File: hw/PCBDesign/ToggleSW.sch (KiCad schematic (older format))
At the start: 8 parts

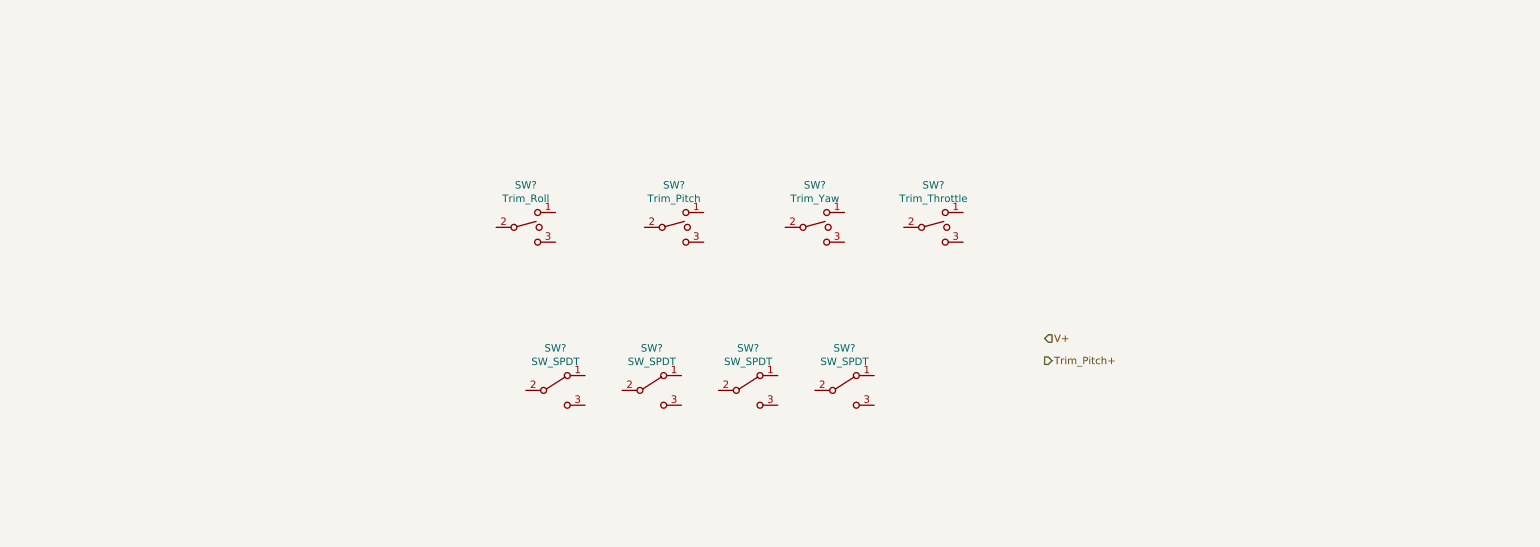
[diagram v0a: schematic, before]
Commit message: Add HMI input circuitry
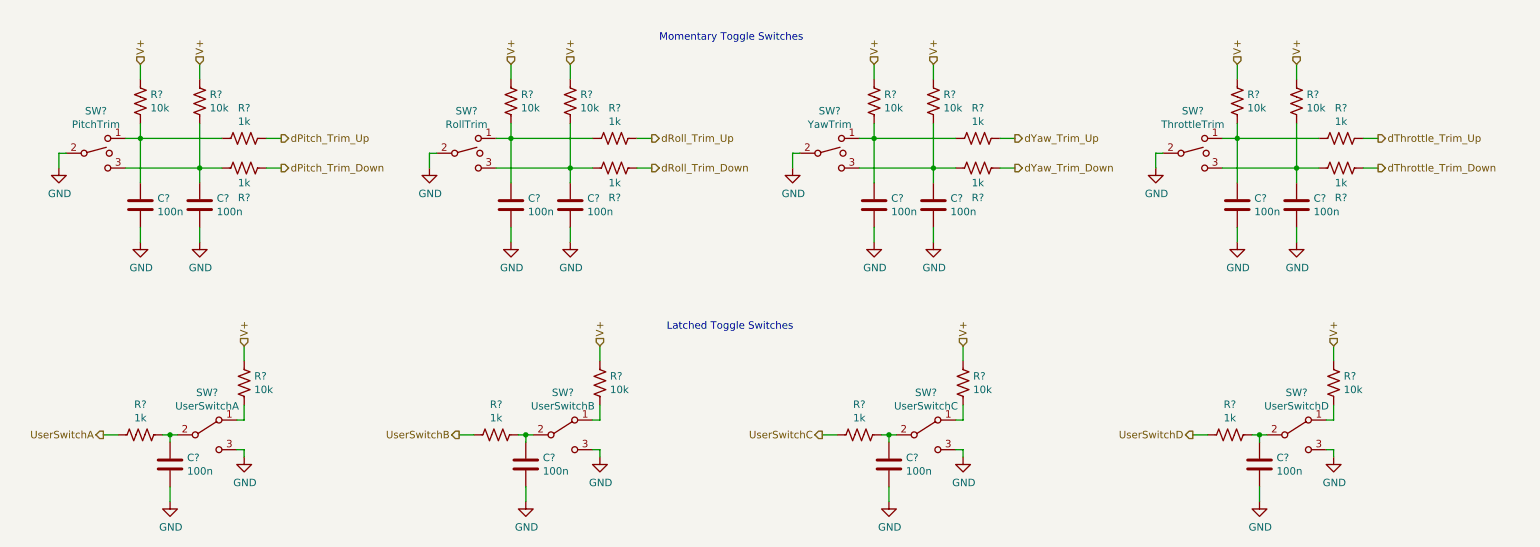
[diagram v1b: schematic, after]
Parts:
- removed SW?: Trim_Pitch, symbol Switch:SW_SPDT_MSM
- removed SW?: Trim_Yaw, symbol Switch:SW_SPDT_MSM
- removed SW?: Trim_Throttle, symbol Switch:SW_SPDT_MSM
- removed SW? (x3): SW_SPDT, symbol Switch:SW_SPDT
- added C? (x12): 100n, symbol Device:C
- added R? (x12): 10k, symbol Device:R_US
- added R? (x12): 1k, symbol Device:R_US
- added SW?: RollTrim, symbol Switch:SW_SPDT_MSM
- added SW?: YawTrim, symbol Switch:SW_SPDT_MSM
- added SW?: ThrottleTrim, symbol Switch:SW_SPDT_MSM
- added SW?: UserSwitchB, symbol Switch:SW_SPDT
- added SW?: UserSwitchC, symbol Switch:SW_SPDT
- added SW?: UserSwitchD, symbol Switch:SW_SPDT
- SW?: value Trim_Roll -> PitchTrim
- SW?: value SW_SPDT -> UserSwitchA
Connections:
- net V+: now also R?.1, R?.1, R?.1, R?.1, R?.1, R?.1, R?.1, R?.1, R?.1, R?.1, R?.1, R?.1
- net at SW?.1: now also C?.1, R?.2, R?.2
- net GND: now reaches SW?.2
- net GND: now also SW?.3 (C), C?.2, C?.2, C?.2, C?.2, C?.2, C?.2, C?.2, C?.2, C?.2, C?.2, C?.2, C?.2, SW?.2, SW?.2, SW?.2, SW?.3 (C), SW?.3 (C), SW?.3 (C)
- net at SW?.3: now also C?.1, R?.1, R?.2
- net at SW?.1 (A): now also R?.2
- net at SW?.2 (B): now also C?.1, R?.1
- new net: C?.1, R?.2, R?.2, SW?.1 (x3)
- new net: C?.1, R?.1, R?.2, SW?.3 (x3)
- new net: R?.2, SW?.1 (A) (x3)
- new net: C?.1, R?.1, SW?.2 (B) (x3)
- new net UserSwitchA: R?.2
- new net UserSwitchB: R?.2
- new net UserSwitchC: R?.2
- new net UserSwitchD: R?.2
- new net dPitch_Trim_Down: R?.2
- new net dPitch_Trim_Up: R?.1
- new net dRoll_Trim_Down: R?.2
- new net dRoll_Trim_Up: R?.1
- new net dThrottle_Trim_Down: R?.2
- new net dThrottle_Trim_Up: R?.1
- new net dYaw_Trim_Down: R?.2
- new net dYaw_Trim_Up: R?.1
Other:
- note added: "Latched Toggle Switches"
- note added: "Momentary Toggle Switches"
- moved on the sheet: SW?

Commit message: Schematic polishing
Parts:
- added J10, J11, J12, J13, J14, J7, J8, J9: Conn_01x03, symbol Connector_Generic:Conn_01x03
- C10, C11, C12, C13, C14, C15, C16, C17, C18, C19, C20, C21: renamed from C?; footprint (none) -> Capacitor_SMD:C_0402_1005Metric; LCSC (none) -> C1525
- R15, R17, R20, R22, R23, R24, R28, R29, R30, R34, R35, R36: renamed from R?; footprint (none) -> Resistor_SMD:R_0402_1005Metric; LCSC (none) -> C25744
- R16, R18, R19, R21, R25, R26, R27, R31, R32, R33, R37, R38: renamed from R?; footprint (none) -> Resistor_SMD:R_0402_1005Metric; LCSC (none) -> C11702
- gave numbers to parts that had none: 8
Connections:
- net GND: now also J10.3 (Pin_3), J11.2 (Pin_2), J12.3 (Pin_3), J13.2 (Pin_2), J14.3 (Pin_3), J7.2 (Pin_2), J8.3 (Pin_3), J9.2 (Pin_2)
- net at C10.1, R15.2, R18.2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: now also J7.3 (Pin_3)
- net at C12.1, R17.2, R19.1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: now also J7.1 (Pin_1)
- net at R20.2, SW4.1 (A): now also J8.1 (Pin_1)
- net at C11.1, R16.1, SW4.2 (B): now also J8.2 (Pin_2)
- net at C13.1, R22.2, R25.2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: now also J9.3 (Pin_3)
- net at C15.1, R23.2, R26.1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: now also J9.1 (Pin_1)
- net at C16.1, R28.2, R31.2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: now also J11.3 (Pin_3)
- net at C18.1, R29.2, R32.1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: now also J11.1 (Pin_1)
- net at C19.1, R34.2, R37.2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: now also J13.3 (Pin_3)
- net at C21.1, R35.2, R38.1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: now also J13.1 (Pin_1)
- net at R24.2, SW6.1 (A): now also J10.1 (Pin_1)
- net at C14.1, R21.1, SW6.2 (B): now also J10.2 (Pin_2)
- net at R30.2, SW8.1 (A): now also J12.1 (Pin_1)
- net at C17.1, R27.1, SW8.2 (B): now also J12.2 (Pin_2)
- net at R36.2, SW10.1 (A): now also J14.1 (Pin_1)
- net at C20.1, R33.1, SW10.2 (B): now also J14.2 (Pin_2)

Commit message: Added PCB
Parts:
- J10, J11, J12, J13, J14, J7, J8, J9: footprint (none) -> Connector_JST:JST_PH_S3B-PH-SM4-TB_1x03-1MP_P2.00mm_Horizontal; DigiKey (none) -> 455-1750-2-ND
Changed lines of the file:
@@
 F 0 "J14" H 10030 3592 50  0000 L CNN
 F 1 "Conn_01x03" H 10030 3501 50  0000 L CNN
-F 2 "" H 9950 3550 50  0001 C CNN
+F 2 "Connector_JST:JST_PH_S3B-PH-SM4-TB_1x03-1MP_P2.00mm_Horizontal" H 9950 3550 50  0001 C CNN
 F 3 "~" H 9950 3550 50  0001 C CNN
+F 4 "455-1750-2-ND" H 9950 3550 50  0001 C CNN "DigiKey"
 	1    9950 3550
 	1    0    0    -1
@@
 F 0 "J12" H 7530 3592 50  0000 L CNN
 F 1 "Conn_01x03" H 7530 3501 50  0000 L CNN
-F 2 "" H 7450 3550 50  0001 C CNN
+F 2 "Connector_JST:JST_PH_S3B-PH-SM4-TB_1x03-1MP_P2.00mm_Horizontal" H 7450 3550 50  0001 C CNN
 F 3 "~" H 7450 3550 50  0001 C CNN
+F 4 "455-1750-2-ND" H 7450 3550 50  0001 C CNN "DigiKey"
 	1    7450 3550
 	1    0    0    -1
@@
 F 0 "J10" H 5080 3592 50  0000 L CNN
 F 1 "Conn_01x03" H 5080 3501 50  0000 L CNN
-F 2 "" H 5000 3550 50  0001 C CNN
+F 2 "Connector_JST:JST_PH_S3B-PH-SM4-TB_1x03-1MP_P2.00mm_Horizontal" H 5000 3550 50  0001 C CNN
 F 3 "~" H 5000 3550 50  0001 C CNN
+F 4 "455-1750-2-ND" H 5000 3550 50  0001 C CNN "DigiKey"
 	1    5000 3550
 	1    0    0    -1
@@
 F 0 "J8" H 2680 3592 50  0000 L CNN
 F 1 "Conn_01x03" H 2680 3501 50  0000 L CNN
-F 2 "" H 2600 3550 50  0001 C CNN
+F 2 "Connector_JST:JST_PH_S3B-PH-SM4-TB_1x03-1MP_P2.00mm_Horizontal" H 2600 3550 50  0001 C CNN
 F 3 "~" H 2600 3550 50  0001 C CNN
+F 4 "455-1750-2-ND" H 2600 3550 50  0001 C CNN "DigiKey"
 	1    2600 3550
 	1    0    0    -1
@@
 F 0 "J7" V 1864 930 50  0000 L CNN
 F 1 "Conn_01x03" V 1773 930 50  0000 L CNN
-F 2 "" H 1900 750 50  0001 C CNN
+F 2 "Connector_JST:JST_PH_S3B-PH-SM4-TB_1x03-1MP_P2.00mm_Horizontal" H 1900 750 50  0001 C CNN
 F 3 "~" H 1900 750 50  0001 C CNN
+F 4 "455-1750-2-ND" H 1900 750 50  0001 C CNN "DigiKey"
 	1    1900 750
 	0    1    -1   0
@@
 F 0 "J9" V 4364 930 50  0000 L CNN
 F 1 "Conn_01x03" V 4273 930 50  0000 L CNN
-F 2 "" H 4400 750 50  0001 C CNN
+F 2 "Connector_JST:JST_PH_S3B-PH-SM4-TB_1x03-1MP_P2.00mm_Horizontal" H 4400 750 50  0001 C CNN
 F 3 "~" H 4400 750 50  0001 C CNN
+F 4 "455-1750-2-ND" H 4400 750 50  0001 C CNN "DigiKey"
 	1    4400 750
 	0    1    -1   0
@@
 F 0 "J11" V 6814 930 50  0000 L CNN
 F 1 "Conn_01x03" V 6723 930 50  0000 L CNN
-F 2 "" H 6850 750 50  0001 C CNN
+F 2 "Connector_JST:JST_PH_S3B-PH-SM4-TB_1x03-1MP_P2.00mm_Horizontal" H 6850 750 50  0001 C CNN
 F 3 "~" H 6850 750 50  0001 C CNN
+F 4 "455-1750-2-ND" H 6850 750 50  0001 C CNN "DigiKey"
 	1    6850 750
 	0    1    -1   0
@@
 F 0 "J13" V 9264 930 50  0000 L CNN
 F 1 "Conn_01x03" V 9173 930 50  0000 L CNN
-F 2 "" H 9300 750 50  0001 C CNN
+F 2 "Connector_JST:JST_PH_S3B-PH-SM4-TB_1x03-1MP_P2.00mm_Horizontal" H 9300 750 50  0001 C CNN
 F 3 "~" H 9300 750 50  0001 C CNN
+F 4 "455-1750-2-ND" H 9300 750 50  0001 C CNN "DigiKey"
 	1    9300 750
 	0    1    -1   0

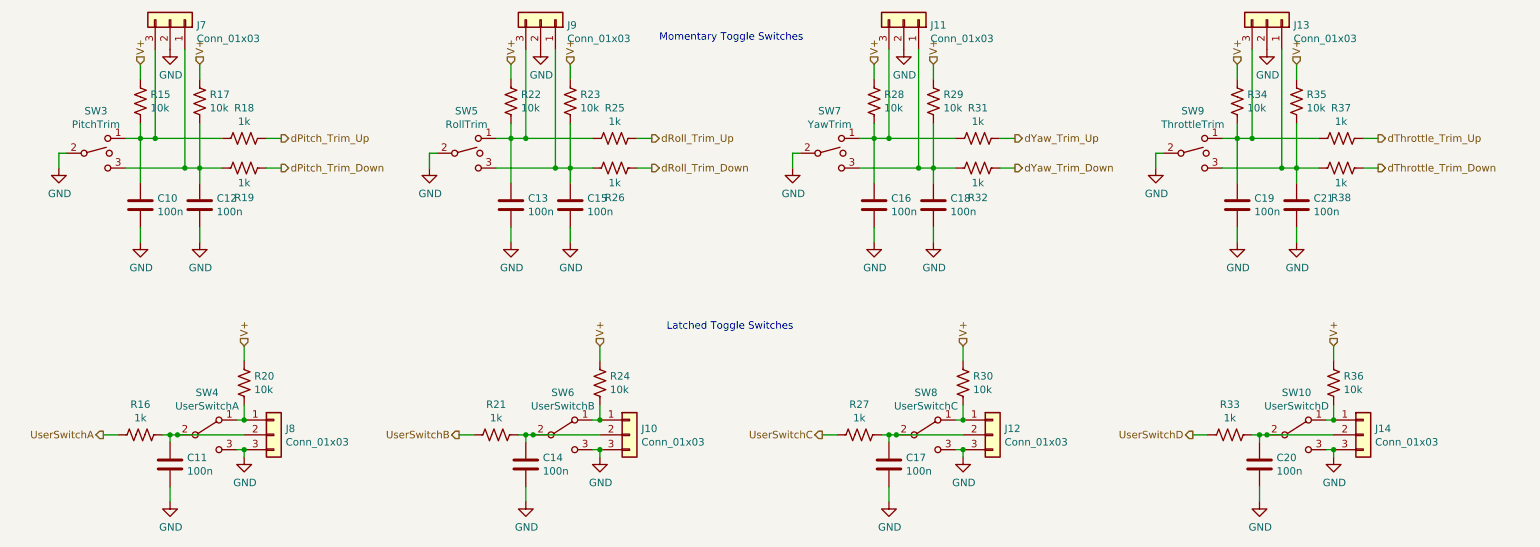
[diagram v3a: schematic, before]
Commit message: Laid out power section
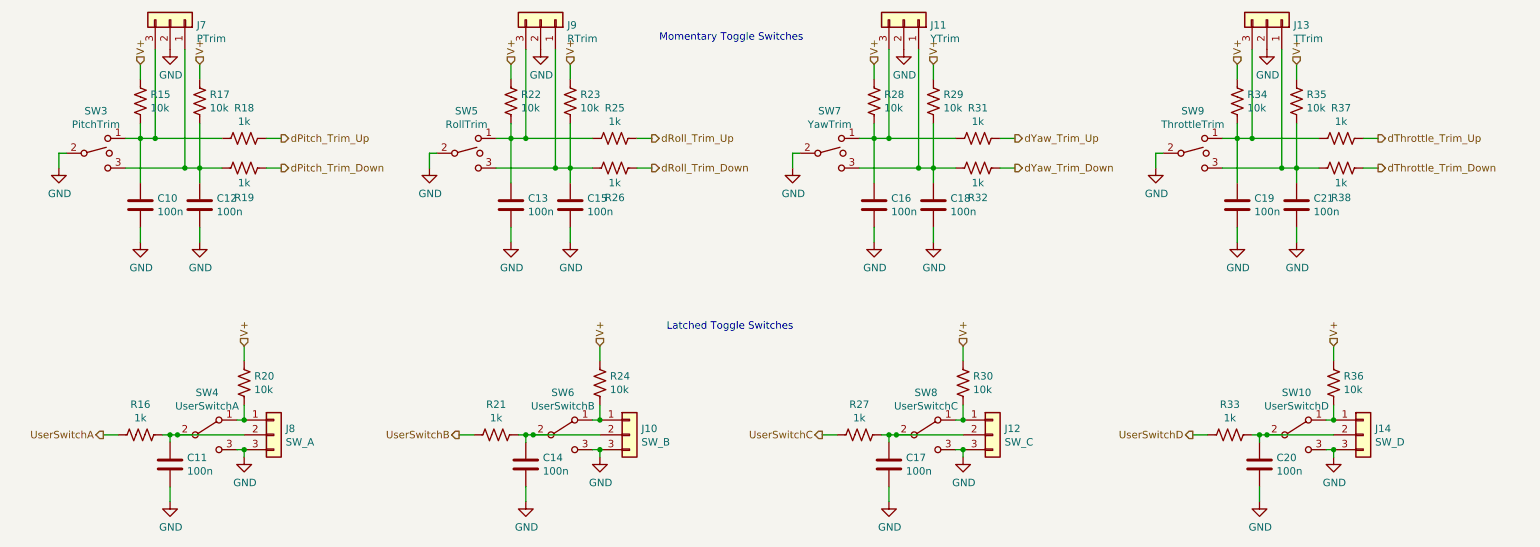
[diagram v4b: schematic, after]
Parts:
- J10: value Conn_01x03 -> SW_B
- J11: value Conn_01x03 -> YTrim
- J12: value Conn_01x03 -> SW_C
- J13: value Conn_01x03 -> TTrim
- J14: value Conn_01x03 -> SW_D
- J7: value Conn_01x03 -> PTrim
- J8: value Conn_01x03 -> SW_A
- J9: value Conn_01x03 -> RTrim
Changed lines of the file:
@@
 P 9950 3550
 F 0 "J14" H 10030 3592 50  0000 L CNN
-F 1 "Conn_01x03" H 10030 3501 50  0000 L CNN
+F 1 "SW_D" H 10030 3501 50  0000 L CNN
 F 2 "Connector_JST:JST_PH_S3B-PH-SM4-TB_1x03-1MP_P2.00mm_Horizontal" H 9950 3550 50  0001 C CNN
 F 3 "~" H 9950 3550 50  0001 C CNN
@@
 P 7450 3550
 F 0 "J12" H 7530 3592 50  0000 L CNN
-F 1 "Conn_01x03" H 7530 3501 50  0000 L CNN
+F 1 "SW_C" H 7530 3501 50  0000 L CNN
 F 2 "Connector_JST:JST_PH_S3B-PH-SM4-TB_1x03-1MP_P2.00mm_Horizontal" H 7450 3550 50  0001 C CNN
 F 3 "~" H 7450 3550 50  0001 C CNN
@@
 P 5000 3550
 F 0 "J10" H 5080 3592 50  0000 L CNN
-F 1 "Conn_01x03" H 5080 3501 50  0000 L CNN
+F 1 "SW_B" H 5080 3501 50  0000 L CNN
 F 2 "Connector_JST:JST_PH_S3B-PH-SM4-TB_1x03-1MP_P2.00mm_Horizontal" H 5000 3550 50  0001 C CNN
 F 3 "~" H 5000 3550 50  0001 C CNN
@@
 P 2600 3550
 F 0 "J8" H 2680 3592 50  0000 L CNN
-F 1 "Conn_01x03" H 2680 3501 50  0000 L CNN
+F 1 "SW_A" H 2680 3501 50  0000 L CNN
 F 2 "Connector_JST:JST_PH_S3B-PH-SM4-TB_1x03-1MP_P2.00mm_Horizontal" H 2600 3550 50  0001 C CNN
 F 3 "~" H 2600 3550 50  0001 C CNN
@@
 P 1900 750
 F 0 "J7" V 1864 930 50  0000 L CNN
-F 1 "Conn_01x03" V 1773 930 50  0000 L CNN
+F 1 "PTrim" V 1773 930 50  0000 L CNN
 F 2 "Connector_JST:JST_PH_S3B-PH-SM4-TB_1x03-1MP_P2.00mm_Horizontal" H 1900 750 50  0001 C CNN
 F 3 "~" H 1900 750 50  0001 C CNN
@@
 P 4400 750
 F 0 "J9" V 4364 930 50  0000 L CNN
-F 1 "Conn_01x03" V 4273 930 50  0000 L CNN
+F 1 "RTrim" V 4273 930 50  0000 L CNN
 F 2 "Connector_JST:JST_PH_S3B-PH-SM4-TB_1x03-1MP_P2.00mm_Horizontal" H 4400 750 50  0001 C CNN
 F 3 "~" H 4400 750 50  0001 C CNN
@@
 P 6850 750
 F 0 "J11" V 6814 930 50  0000 L CNN
-F 1 "Conn_01x03" V 6723 930 50  0000 L CNN
+F 1 "YTrim" V 6723 930 50  0000 L CNN
 F 2 "Connector_JST:JST_PH_S3B-PH-SM4-TB_1x03-1MP_P2.00mm_Horizontal" H 6850 750 50  0001 C CNN
 F 3 "~" H 6850 750 50  0001 C CNN
@@
 P 9300 750
 F 0 "J13" V 9264 930 50  0000 L CNN
-F 1 "Conn_01x03" V 9173 930 50  0000 L CNN
+F 1 "TTrim" V 9173 930 50  0000 L CNN
 F 2 "Connector_JST:JST_PH_S3B-PH-SM4-TB_1x03-1MP_P2.00mm_Horizontal" H 9300 750 50  0001 C CNN
 F 3 "~" H 9300 750 50  0001 C CNN

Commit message: HW updates. Testing out SPIFFS
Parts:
- J10, J11, J12, J13, J14, J7, J8, J9: footprint Connector_JST:JST_PH_S3B-PH-SM4-TB_1x03-1MP_P2.00mm_Horizontal -> Connector_JST:JST_PH_B3B-PH-SM4-TB_1x03-1MP_P2.00mm_Vertical; DigiKey 455-1750-2-ND -> 455-1735-2-ND
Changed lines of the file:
@@
 F 0 "J14" H 10030 3592 50  0000 L CNN
 F 1 "SW_D" H 10030 3501 50  0000 L CNN
-F 2 "Connector_JST:JST_PH_S3B-PH-SM4-TB_1x03-1MP_P2.00mm_Horizontal" H 9950 3550 50  0001 C CNN
+F 2 "Connector_JST:JST_PH_B3B-PH-SM4-TB_1x03-1MP_P2.00mm_Vertical" H 9950 3550 50  0001 C CNN
 F 3 "~" H 9950 3550 50  0001 C CNN
-F 4 "455-1750-2-ND" H 9950 3550 50  0001 C CNN "DigiKey"
+F 4 "455-1735-2-ND" H 9950 3550 50  0001 C CNN "DigiKey"
 	1    9950 3550
 	1    0    0    -1
@@
 F 0 "J12" H 7530 3592 50  0000 L CNN
 F 1 "SW_C" H 7530 3501 50  0000 L CNN
-F 2 "Connector_JST:JST_PH_S3B-PH-SM4-TB_1x03-1MP_P2.00mm_Horizontal" H 7450 3550 50  0001 C CNN
+F 2 "Connector_JST:JST_PH_B3B-PH-SM4-TB_1x03-1MP_P2.00mm_Vertical" H 7450 3550 50  0001 C CNN
 F 3 "~" H 7450 3550 50  0001 C CNN
-F 4 "455-1750-2-ND" H 7450 3550 50  0001 C CNN "DigiKey"
+F 4 "455-1735-2-ND" H 7450 3550 50  0001 C CNN "DigiKey"
 	1    7450 3550
 	1    0    0    -1
@@
 F 0 "J10" H 5080 3592 50  0000 L CNN
 F 1 "SW_B" H 5080 3501 50  0000 L CNN
-F 2 "Connector_JST:JST_PH_S3B-PH-SM4-TB_1x03-1MP_P2.00mm_Horizontal" H 5000 3550 50  0001 C CNN
+F 2 "Connector_JST:JST_PH_B3B-PH-SM4-TB_1x03-1MP_P2.00mm_Vertical" H 5000 3550 50  0001 C CNN
 F 3 "~" H 5000 3550 50  0001 C CNN
-F 4 "455-1750-2-ND" H 5000 3550 50  0001 C CNN "DigiKey"
+F 4 "455-1735-2-ND" H 5000 3550 50  0001 C CNN "DigiKey"
 	1    5000 3550
 	1    0    0    -1
@@
 F 0 "J8" H 2680 3592 50  0000 L CNN
 F 1 "SW_A" H 2680 3501 50  0000 L CNN
-F 2 "Connector_JST:JST_PH_S3B-PH-SM4-TB_1x03-1MP_P2.00mm_Horizontal" H 2600 3550 50  0001 C CNN
+F 2 "Connector_JST:JST_PH_B3B-PH-SM4-TB_1x03-1MP_P2.00mm_Vertical" H 2600 3550 50  0001 C CNN
 F 3 "~" H 2600 3550 50  0001 C CNN
-F 4 "455-1750-2-ND" H 2600 3550 50  0001 C CNN "DigiKey"
+F 4 "455-1735-2-ND" H 2600 3550 50  0001 C CNN "DigiKey"
 	1    2600 3550
 	1    0    0    -1
@@
 F 0 "J7" V 1864 930 50  0000 L CNN
 F 1 "PTrim" V 1773 930 50  0000 L CNN
-F 2 "Connector_JST:JST_PH_S3B-PH-SM4-TB_1x03-1MP_P2.00mm_Horizontal" H 1900 750 50  0001 C CNN
+F 2 "Connector_JST:JST_PH_B3B-PH-SM4-TB_1x03-1MP_P2.00mm_Vertical" H 1900 750 50  0001 C CNN
 F 3 "~" H 1900 750 50  0001 C CNN
-F 4 "455-1750-2-ND" H 1900 750 50  0001 C CNN "DigiKey"
+F 4 "455-1735-2-ND" H 1900 750 50  0001 C CNN "DigiKey"
 	1    1900 750
 	0    1    -1   0
@@
 F 0 "J9" V 4364 930 50  0000 L CNN
 F 1 "RTrim" V 4273 930 50  0000 L CNN
-F 2 "Connector_JST:JST_PH_S3B-PH-SM4-TB_1x03-1MP_P2.00mm_Horizontal" H 4400 750 50  0001 C CNN
+F 2 "Connector_JST:JST_PH_B3B-PH-SM4-TB_1x03-1MP_P2.00mm_Vertical" H 4400 750 50  0001 C CNN
 F 3 "~" H 4400 750 50  0001 C CNN
-F 4 "455-1750-2-ND" H 4400 750 50  0001 C CNN "DigiKey"
+F 4 "455-1735-2-ND" H 4400 750 50  0001 C CNN "DigiKey"
 	1    4400 750
 	0    1    -1   0
@@
 F 0 "J11" V 6814 930 50  0000 L CNN
 F 1 "YTrim" V 6723 930 50  0000 L CNN
-F 2 "Connector_JST:JST_PH_S3B-PH-SM4-TB_1x03-1MP_P2.00mm_Horizontal" H 6850 750 50  0001 C CNN
+F 2 "Connector_JST:JST_PH_B3B-PH-SM4-TB_1x03-1MP_P2.00mm_Vertical" H 6850 750 50  0001 C CNN
 F 3 "~" H 6850 750 50  0001 C CNN
-F 4 "455-1750-2-ND" H 6850 750 50  0001 C CNN "DigiKey"
+F 4 "455-1735-2-ND" H 6850 750 50  0001 C CNN "DigiKey"
 	1    6850 750
 	0    1    -1   0
@@
 F 0 "J13" V 9264 930 50  0000 L CNN
 F 1 "TTrim" V 9173 930 50  0000 L CNN
-F 2 "Connector_JST:JST_PH_S3B-PH-SM4-TB_1x03-1MP_P2.00mm_Horizontal" H 9300 750 50  0001 C CNN
+F 2 "Connector_JST:JST_PH_B3B-PH-SM4-TB_1x03-1MP_P2.00mm_Vertical" H 9300 750 50  0001 C CNN
 F 3 "~" H 9300 750 50  0001 C CNN
-F 4 "455-1750-2-ND" H 9300 750 50  0001 C CNN "DigiKey"
+F 4 "455-1735-2-ND" H 9300 750 50  0001 C CNN "DigiKey"
 	1    9300 750
 	0    1    -1   0
